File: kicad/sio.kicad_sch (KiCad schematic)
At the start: 2 parts, among them U4 Z80 SIO3

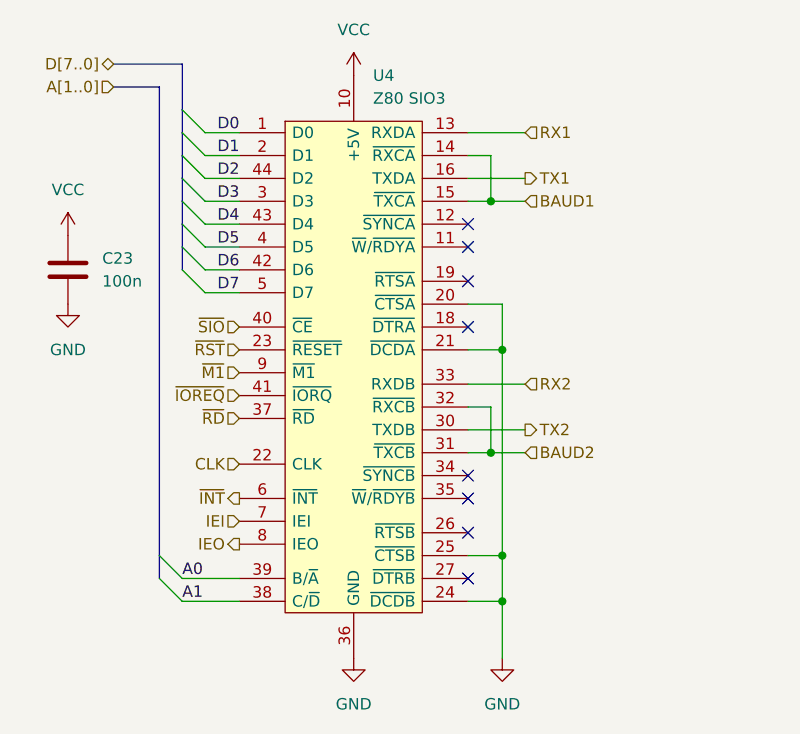
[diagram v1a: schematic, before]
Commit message: HW: fix floating SYNC pins of SIO
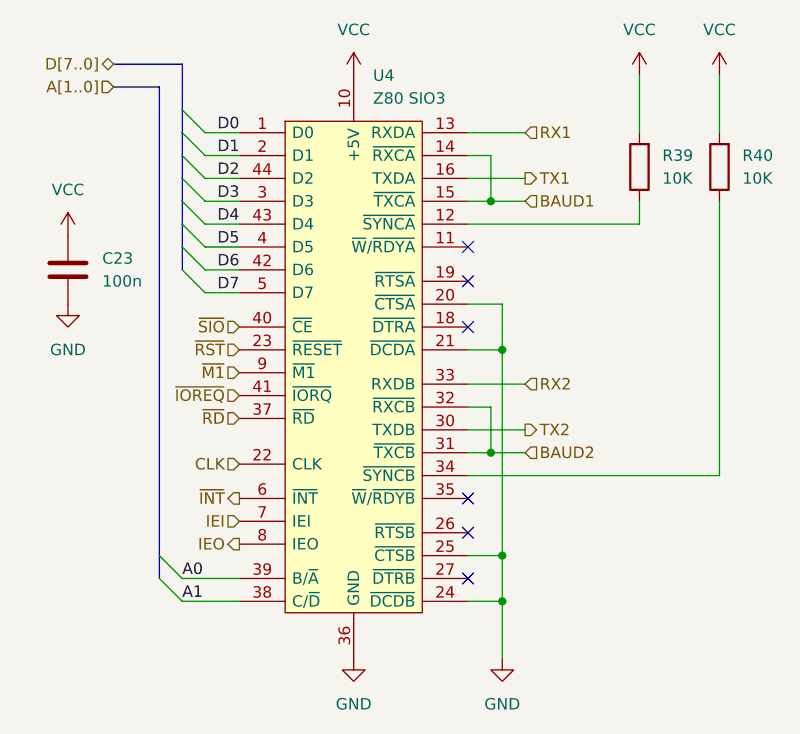
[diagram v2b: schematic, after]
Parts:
- added R39, R40: 10K, Resistor_SMD:R_0805_2012Metric, symbol Device:R
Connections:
- net VCC: now also R39.2, R40.2
- net at U4.12 (~{SYNCA}): now also R39.1
- net at U4.34 (~{SYNCB}): now also R40.1
- no-connect marks 8 -> 6
